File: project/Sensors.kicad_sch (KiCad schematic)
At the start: 15 parts, among them IC1 APDS-9306-065, IC12 BMP581, IC13 BME688, IC14 LIS2MDLTR, IC8 BMI270

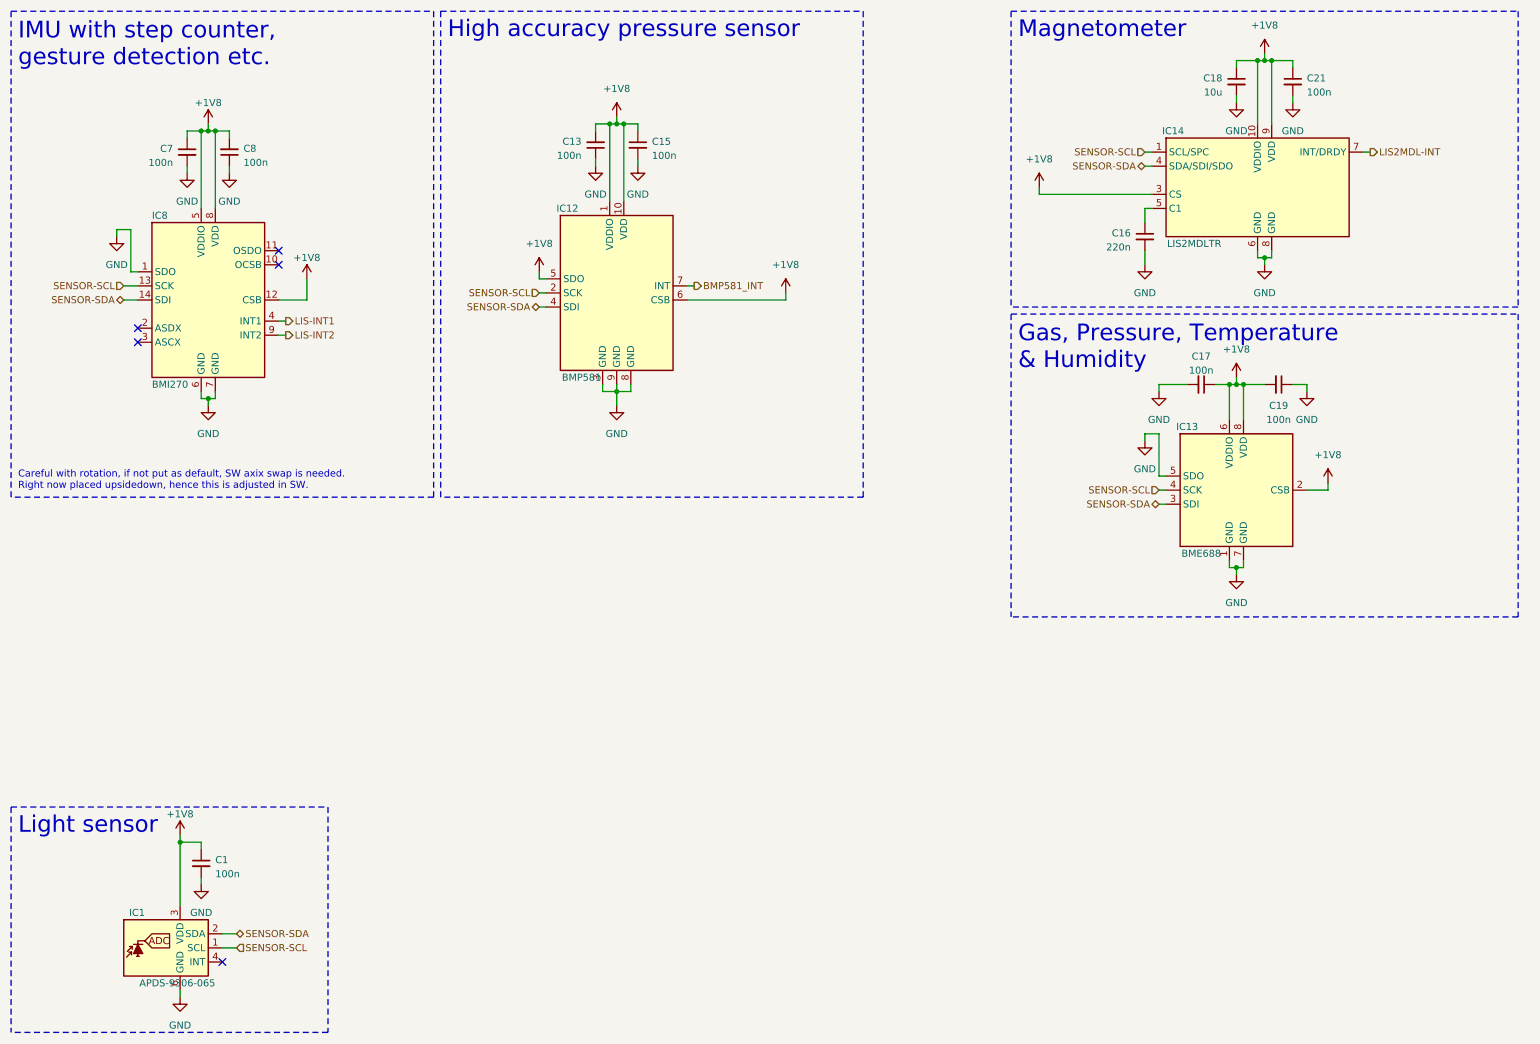
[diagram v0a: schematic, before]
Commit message: - Add QR code library with link to the project - Change ISET resistor to 12k - Replace light sensor footprint with a version from our KiCad library - Rename the inner copper layers - Add KiBot file for production file generation - Import nPM1300 from test project - Remove pull down resistor from vibration driver IC enable - Split schematics into hierarical schematics - Add PCB variant for reduced sensor board - Add I2S microphone - Update all symbols and footprints
Signed-off-by: Daniel Kampert <DanielKampert@kampis-elektroecke.de>
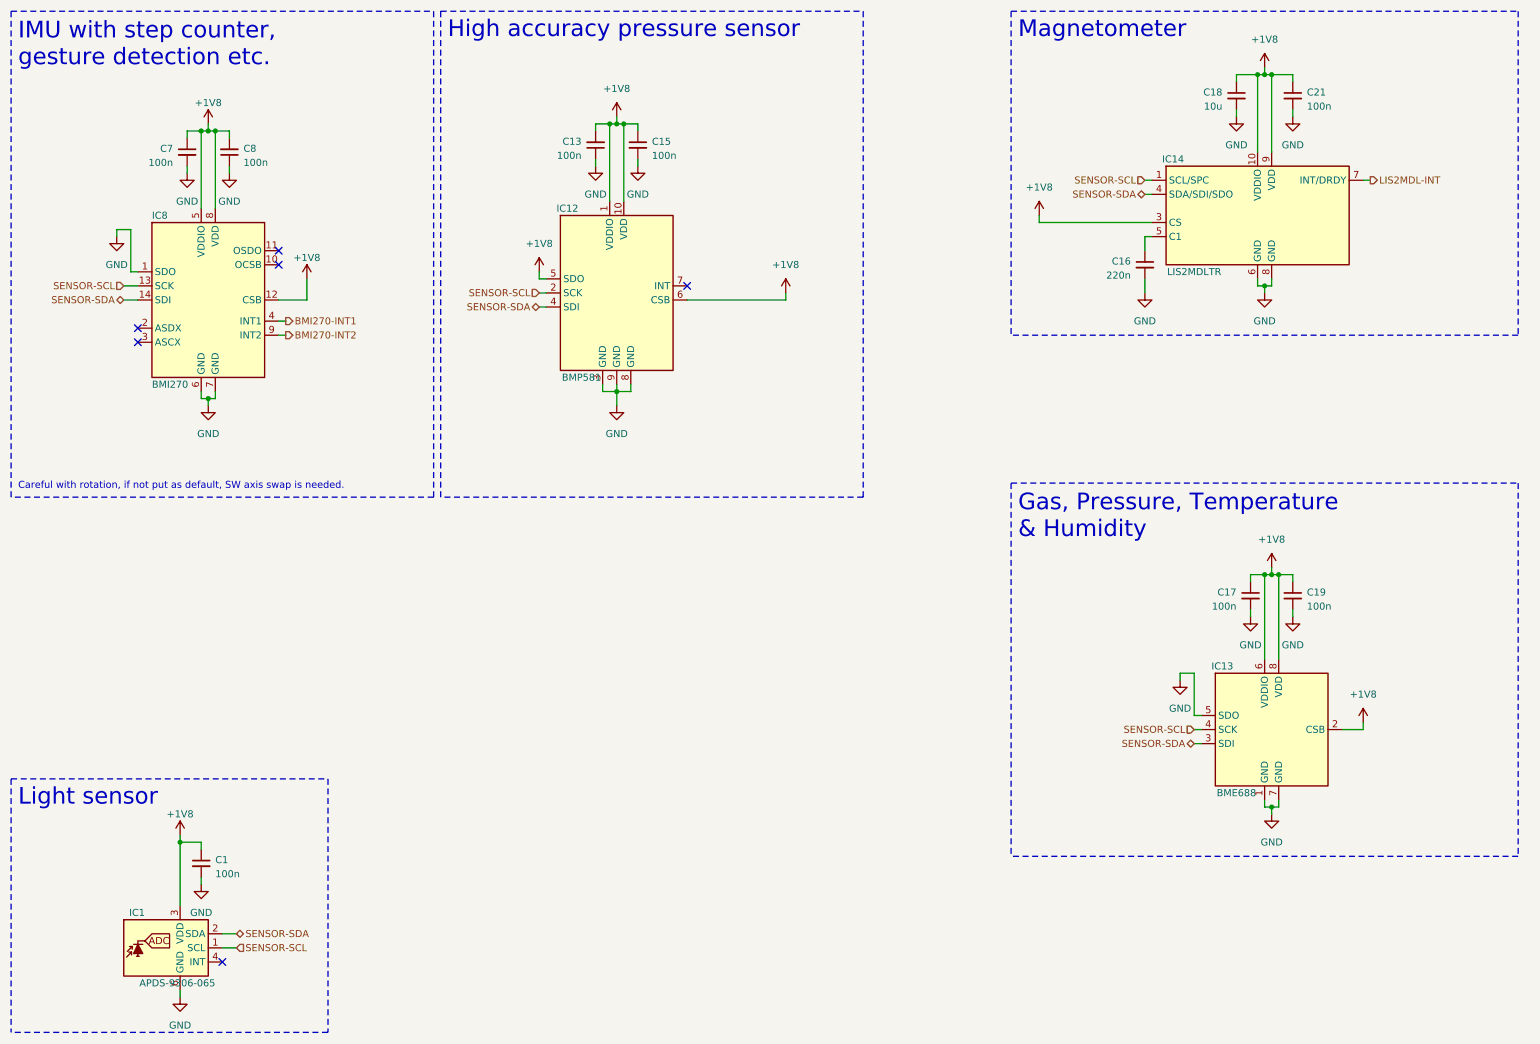
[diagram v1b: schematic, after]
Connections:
- net +1V8: now also C19.1; no longer C19.2
- net GND: now also C19.2; no longer C19.1
- net BMP581_INT: no longer names the net of IC12.7 (INT)
- net LIS-INT1 renamed BMI270-INT1
- net LIS-INT2 renamed BMI270-INT2
- no-connect marks 5 -> 6
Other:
- note added: "Careful with rotation, if not put as default, SW axis swap is needed."
- note removed: "Careful with rotation, if not put as default, SW axix swap is needed. Right now placed upsidedown, hence this is adjusted in SW."
- moved on the sheet: C16, C17, C18, C19, C21, IC13, IC14

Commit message: - Add QR code library with link to the project - Change ISET resistor to 12k - Replace light sensor footprint with a version from our KiCad library - Rename the inner copper layers - Add KiBot file for production file generation - Import nPM1300 from test project - Remove pull down resistor from vibration driver IC enable - Split schematics into hierarical schematics - Add PCB variant for reduced sensor board - Add I2S microphone - Update all symbols and footprints - Move BTN_2 from P0.30 to P1.10 - Move BTN_3 from P1.12 to P0.31 - Move DRV_VIB_EN from P1.14 to P1.05 - Move BMI270_IN1 from P0.21 to P1.08 - Move BMI270_IN2 from P0.19 to P1.04 - Move DRV_VIB_PWM from P1.15 to P1.05 - Move DRV_VIB_EN from P1.05 to P1.15 - Move BTN_4 from P1.06 to P0.26 - Replace ESDALC6V1W5 with ESDALC6V1P5 - Add USB support (experimental) - Add marker for display cable orientation - Add markers for better IC placements - Replace the flash memory with WSON-8 variant to allow 64 MB devices - Remove old PCBWay documentation
Signed-off-by: Daniel Kampert <DanielKampert@kampis-elektroecke.de>
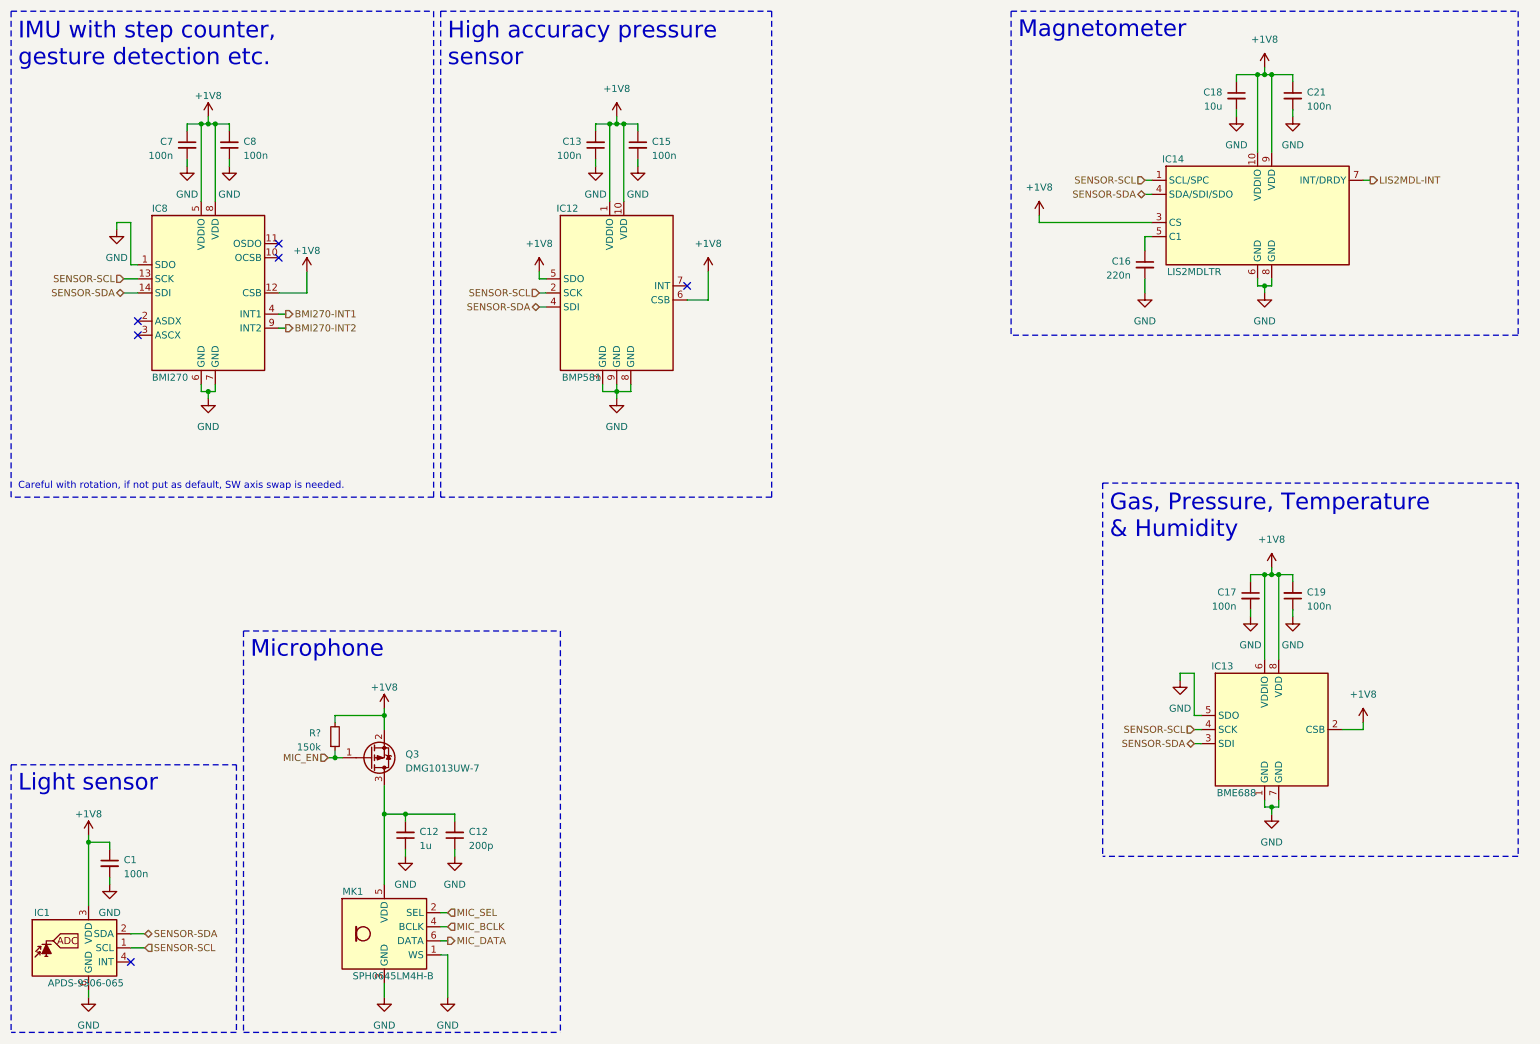
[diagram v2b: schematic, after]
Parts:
- added C12: 1u, Capacitor_SMD:C_0603_1608Metric, symbol Device:C_Small
- added C12: 200p, Capacitor_SMD:C_0603_1608Metric, symbol Device:C_Small
- added MK1: SPH0645LM4H-B, Knowles:SPH0645LM4H-6_3.5x2.65mm, symbol Knowles:SPH0645LM4H-B
- added Q3: DMG1013UW-7, Package_TO_SOT_SMD:SOT-323_SC-70, symbol Diodes Incorporated:DMG1013UW-7
- added R?: 150k, Resistor_SMD:R_0603_1608Metric, symbol Device:R_Small
- C18: Mfr. Murata Electronics -> KYOCERA AVX; Mfr. No. GRM188R61A106MAALD -> CM105X5R106M25AT; Order Number 81-GRM188R61A106MALD -> 346-CM105X5R106M25AT
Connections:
- net +1V8: now also C19.2, Q3.2 (S), R?.2; no longer C19.1
- net GND: now also C19.1, C12.1, C12.1, MK1.1 (WS), MK1.3 (GND); no longer C19.2
- new net: C12.2, C12.2, MK1.5 (VDD), Q3.3 (D)
- new net MIC_BCLK: MK1.4 (BCLK)
- new net MIC_DATA: MK1.6 (DATA)
- new net MIC_EN: Q3.1 (G), R?.1
- new net MIC_SEL: MK1.2 (SEL)
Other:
- note added: "Microphone"
- moved on the sheet: C1, C19, C7, C8, IC1, IC8

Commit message: - Remove S1, S2 and S4 from Sensor variant - Remove microphone from Sensor variant - Update symbols - Add missing supply chain documentation - Update KiBot template to the newest version
Signed-off-by: Daniel Kampert <DanielKampert@kampis-elektroecke.de>
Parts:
- Q3: CONFIG (none) -> -ENV
- R?: CONFIG (none) -> -ENV; Mfr. No. (none) -> RC0603FR-07150KL; Order Number (none) -> 603-RC0603FR-07150KL
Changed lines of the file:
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@@
       (effects (font (size 1.27 1.27)) hide)
     )
-    (property "CONFIG" "" (at 80.01 147.32 0)
+    (property "CONFIG" "-ENV" (at 80.01 147.32 0)
       (effects (font (size 1.27 1.27)) hide)
     )
@@
       (effects (font (size 1.27 1.27)) hide)
     )
-    (property "Mfr. No." "" (at 71.12 143.51 0)
-      (effects (font (size 1.27 1.27)) hide)
-    )
-    (property "Order Number" "" (at 71.12 143.51 0)
-      (effects (font (size 1.27 1.27)) hide)
-    )
-    (property "CONFIG" "" (at 71.12 143.51 0)
-      (effects (font (size 1.27 1.27)) hide)
-    )
+    (property "Mfr. No." "RC0603FR-07150KL" (at 71.12 143.51 0)
+      (effects (font (size 1.27 1.27)) hide)
+    )
+    (property "Order Number" "603-RC0603FR-07150KL" (at 71.12 143.51 0)
+      (effects (font (size 1.27 1.27)) hide)
+    )
+    (property "CONFIG" "-ENV" (at 71.12 143.51 0)
+      (effects (font (size 1.27 1.27)) hide)
+    )

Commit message: - Remove old documentation - Update libraries - Rename signals - Update CHANGELOG
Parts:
- IC3: renamed from IC8; footprint Package_LGA:LGA-14_3x2.5mm_P0.5mm_LayoutBorder3x4y -> Package_LGA_Kampi:Bosch_LGA-14_3x2.5mm_P0.5mm_LayoutBorder3x4y
- gave numbers to parts that had none: 1
- renumbered C7 to C11, C1 to C12, C8 to C13, C13 to C14, C18 to C17, C17 to C18, C21 to C19, C19 to C20, C12 to C23, C12 to C24, IC1 to IC2, IC12 to IC4, IC14 to IC5, IC13 to IC6
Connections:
- net MIC_BCLK renamed MIC-BCLK
- net MIC_DATA renamed MIC-DATA
- net MIC_EN renamed MIC-EN
- net MIC_SEL renamed MIC-SEL
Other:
- moved on the sheet: C17, C19

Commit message: Update README, replace current measurement jumper with 0402 resistor on TOP side, update footprints and symbols
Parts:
- renumbered C12 to C11, C11 to C12, C23 to C14, C24 to C15, C14 to C16, C15 to C17, C16 to C18, C17 to C19, C18 to C20, C19 to C21, C20 to C22, Q3 to Q1, R14 to R4

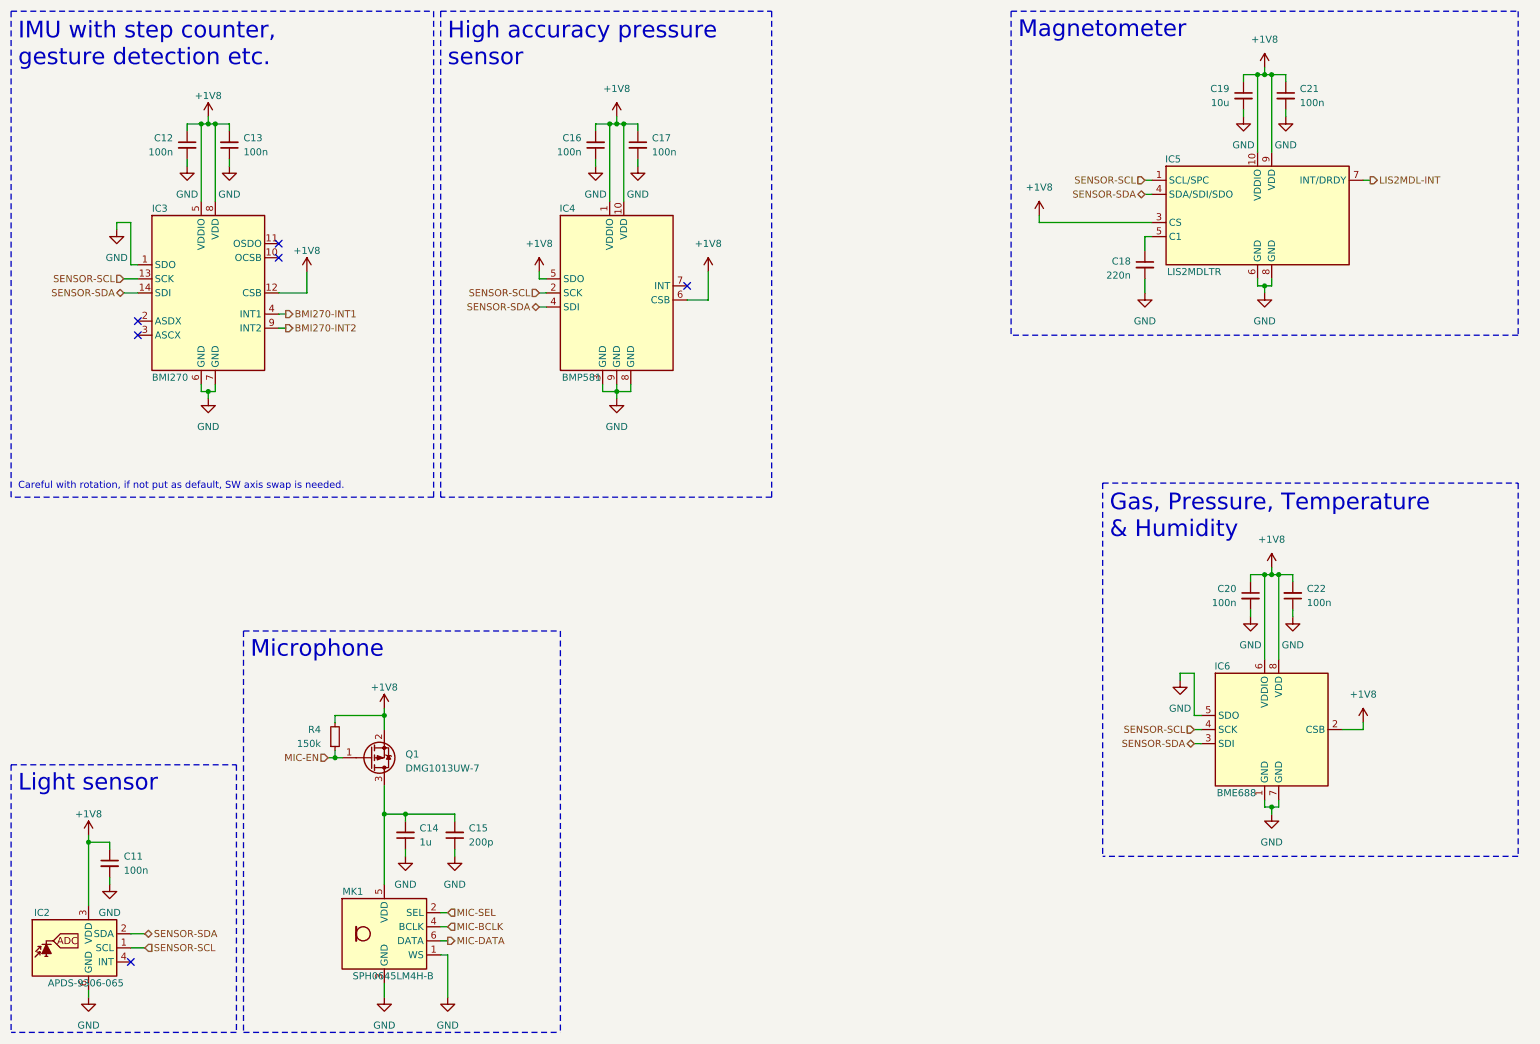
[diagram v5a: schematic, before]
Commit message: Replace I2C mic with SPK0641HT4H-1
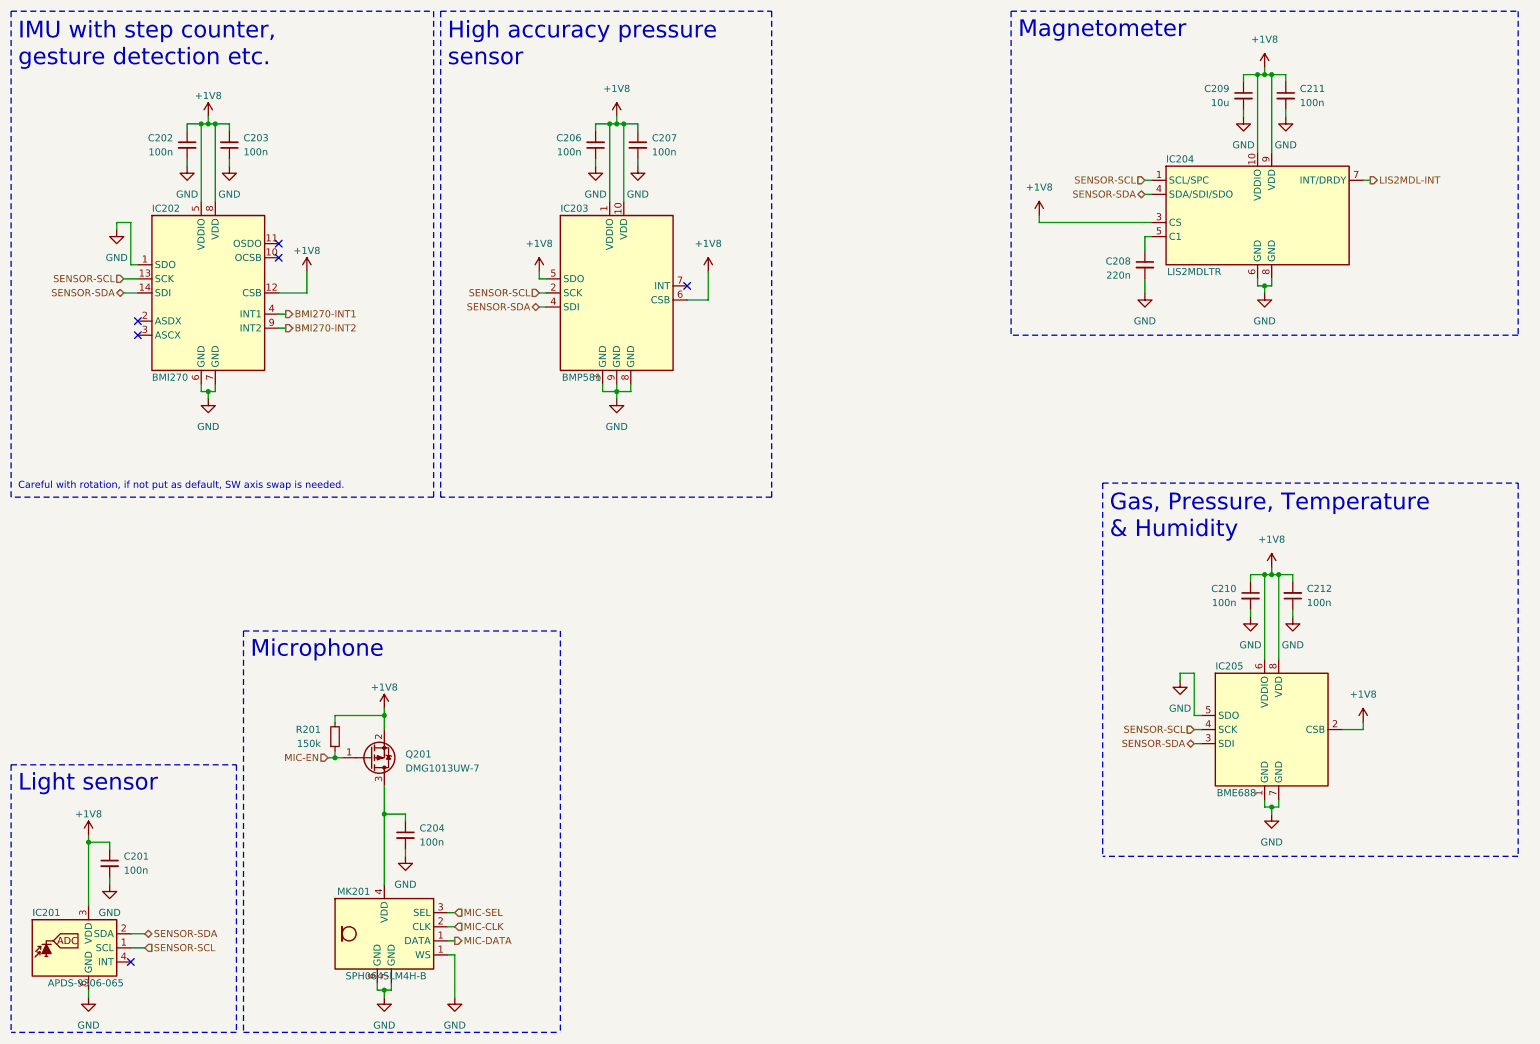
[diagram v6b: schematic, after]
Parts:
- removed C14: 1u, Capacitor_SMD:C_0603_1608Metric, symbol Device:C_Small
- removed C15: 200p, Capacitor_SMD:C_0603_1608Metric, symbol Device:C_Small
- added C204: 100n, Capacitor_SMD:C_0603_1608Metric, symbol Device:C_Small
- MK201: renamed from MK1; footprint Knowles:SPH0645LM4H-6_3.5x2.65mm -> Knowles:SPK0641HT4H-1; symbol Knowles:SPH0645LM4H-B -> Knowles:SPK0641HT4H-1; Mfr. No. SPH0645LM4H-B -> SPK0641HT4H-1; Order Number 721-SPH0645LM4H-B -> 721-SPK0641HT4H-1
- renumbered C11 to C201, C12 to C202, C13 to C203, C16 to C206, C17 to C207, C18 to C208, C19 to C209, C20 to C210, C21 to C211, C22 to C212, IC2 to IC201, IC3 to IC202, IC4 to IC203, IC5 to IC204, IC6 to IC205, Q1 to Q201, R4 to R201
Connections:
- net MIC-BCLK is gone; now on an unnamed net: MK201.4 (VDD)
- net GND: now also MK201.5 (GND), MK201.6 (GND), MK201.7 (GND), MK201.8 (GND), C204.2; no longer MK201.3 (GND)
- net MIC-DATA: now also MK201.1 (WS); no longer MK201.6 (DATA)
- net MIC-SEL: now also MK201.3 (SEL); no longer MK201.2 (SEL)
- net at Q201.3 (D): now also C204.1; no longer MK201.5 (VDD)
- new net MIC-CLK: MK201.2 (CLK)
